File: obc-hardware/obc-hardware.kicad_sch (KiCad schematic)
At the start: 4 parts

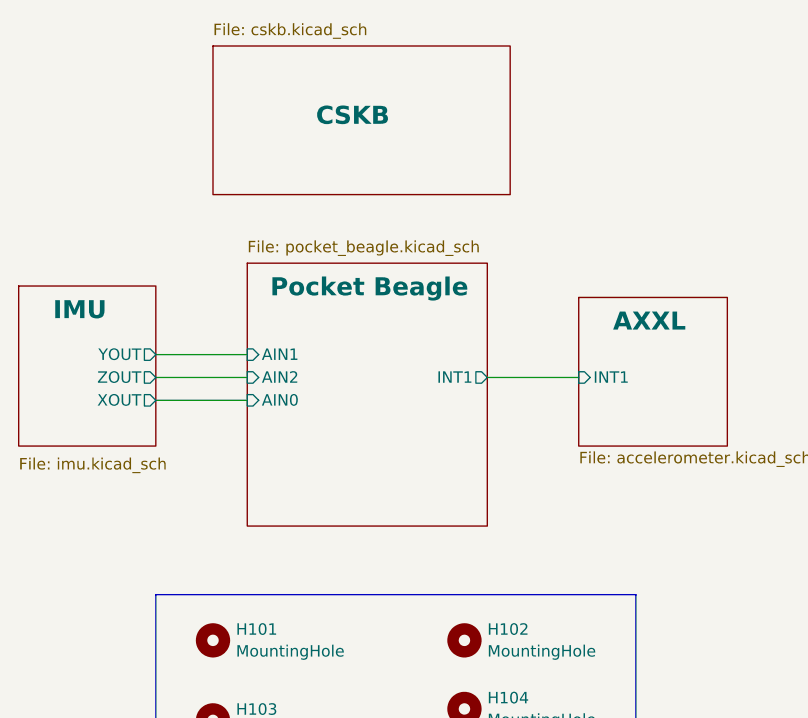
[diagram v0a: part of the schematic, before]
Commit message: added GPIO for payload
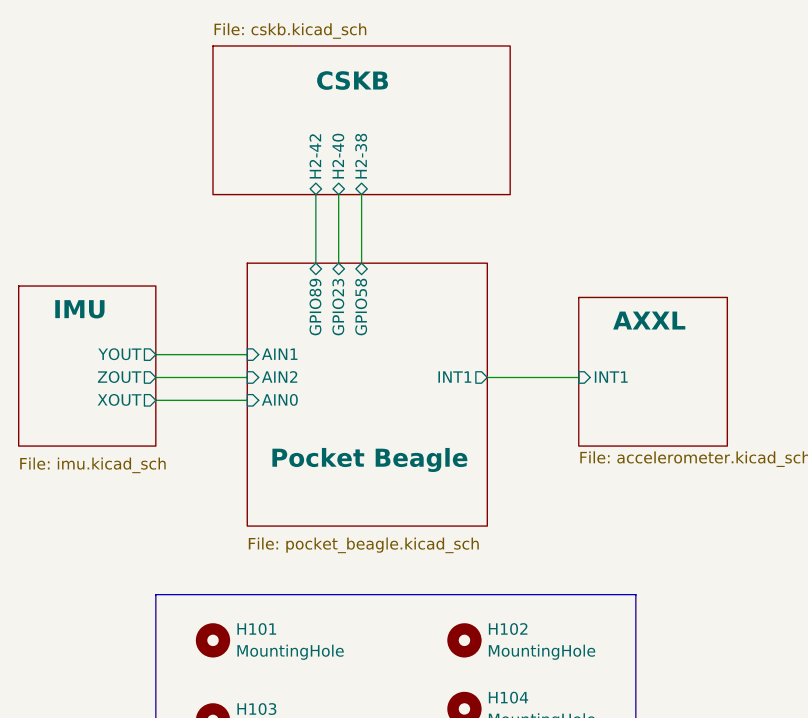
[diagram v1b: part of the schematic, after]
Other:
- sheet CSKB ports: added H2-38, H2-40, H2-42; removed none
- sheet Pocket Beagle ports: added GPIO23, GPIO58, GPIO89; removed none
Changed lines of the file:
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@@
+    (stroke (width 0) (type default))
+  )
+  (wire (pts (xy 135.89 69.85) (xy 135.89 77.47))
     (stroke (width 0) (type default))
   )
@@
   )
   (wire (pts (xy 118.11 87.63) (xy 128.27 87.63))
+    (stroke (width 0) (type default))
+  )
+  (wire (pts (xy 140.97 69.85) (xy 140.97 77.47))
+    (stroke (width 0) (type default))
+  )
+  (wire (pts (xy 138.43 69.85) (xy 138.43 77.47))
     (stroke (width 0) (type default))
   )
@@
     (stroke (width 0.1524) (type solid))
     (fill (color 0 0 0 0.0000))
-    (property "Sheetname" "Pocket Beagle" (at 130.81 81.28 0)
+    (property "Sheetname" "Pocket Beagle" (at 130.81 100.33 0)
       (effects (font (size 2 2) bold) (justify left bottom))
     )
-    (property "Sheetfile" "pocket_beagle.kicad_sch" (at 128.27 74.93 0)
+    (property "Sheetfile" "pocket_beagle.kicad_sch" (at 128.27 107.95 0)
       (effects (font (size 1.27 1.27)) (justify left top))
     )
@@
       (effects (font (size 1.27 1.27)) (justify right))
     )
+    (pin "GPIO89" bidirectional (at 135.89 77.47 90)
+      (effects (font (size 1.27 1.27)) (justify right))
+    )
+    (pin "GPIO23" bidirectional (at 138.43 77.47 90)
+      (effects (font (size 1.27 1.27)) (justify right))
+    )
+    (pin "GPIO58" bidirectional (at 140.97 77.47 90)
+      (effects (font (size 1.27 1.27)) (justify right))
+    )
     (instances
       (project "obc-hardware"
@@
     (stroke (width 0.1524) (type solid))
     (fill (color 0 0 0 0.0000))
-    (property "Sheetname" "CSKB" (at 135.89 62.23 0)
+    (property "Sheetname" "CSKB" (at 135.89 58.42 0)
       (effects (font (size 2 2) bold) (justify left bottom))
     )
@@
       (effects (font (size 1.27 1.27)) (justify left top))
     )
+    (pin "H2-40" bidirectional (at 138.43 69.85 270)
+      (effects (font (size 1.27 1.27)) (justify left))
+    )
+    (pin "H2-42" bidirectional (at 135.89 69.85 270)
+      (effects (font (size 1.27 1.27)) (justify left))
+    )
+    (pin "H2-38" bidirectional (at 140.97 69.85 270)
+      (effects (font (size 1.27 1.27)) (justify left))
+    )
     (instances

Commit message: added test points
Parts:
- added TP101, TP102, TP103, TP104, TP105, TP106, TP107, TP108, TP109, TP110, TP111, TP112: TestPoint, TestPoint:TestPoint_THTPad_1.0x1.0mm_Drill0.5mm, symbol Connector:TestPoint
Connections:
- new net Pocket Beagle/AIN3: TP105.1
- new net Pocket Beagle/AIN4: TP104.1
- new net Pocket Beagle/AIN5: TP106.1
- new net Pocket Beagle/BAT.VIN: TP101.1
- new net Pocket Beagle/GPIO26: TP110.1
- new net Pocket Beagle/GPIO27: TP111.1
- new net Pocket Beagle/GPIO45: TP112.1
- new net Pocket Beagle/PRU0.1: TP107.1
- new net Pocket Beagle/PRU0.2: TP108.1
- new net Pocket Beagle/PWM0A: TP109.1
- new net Pocket Beagle/VOUT-24: TP102.1
- new net Pocket Beagle/VOUT-49: TP103.1
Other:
- sheet Pocket Beagle ports: added AIN3, AIN4, AIN5, BAT.VIN, GPIO26, GPIO27, GPIO45, PRU0.1, PRU0.2, PWM0A, VOUT-24, VOUT-49; removed none
- moved on the sheet: H101, H102, H103, H104
